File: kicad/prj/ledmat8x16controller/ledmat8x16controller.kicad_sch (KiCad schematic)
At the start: 13 parts, among them J1 Conn_02x08_Odd_Even, J2 Conn_01x02, J3 Conn_01x02_Pin, J4 Conn_01x02_Pin, J6 Conn_01x02_Pin, J8 Conn_01x09_Pin, SW2 SW_Push

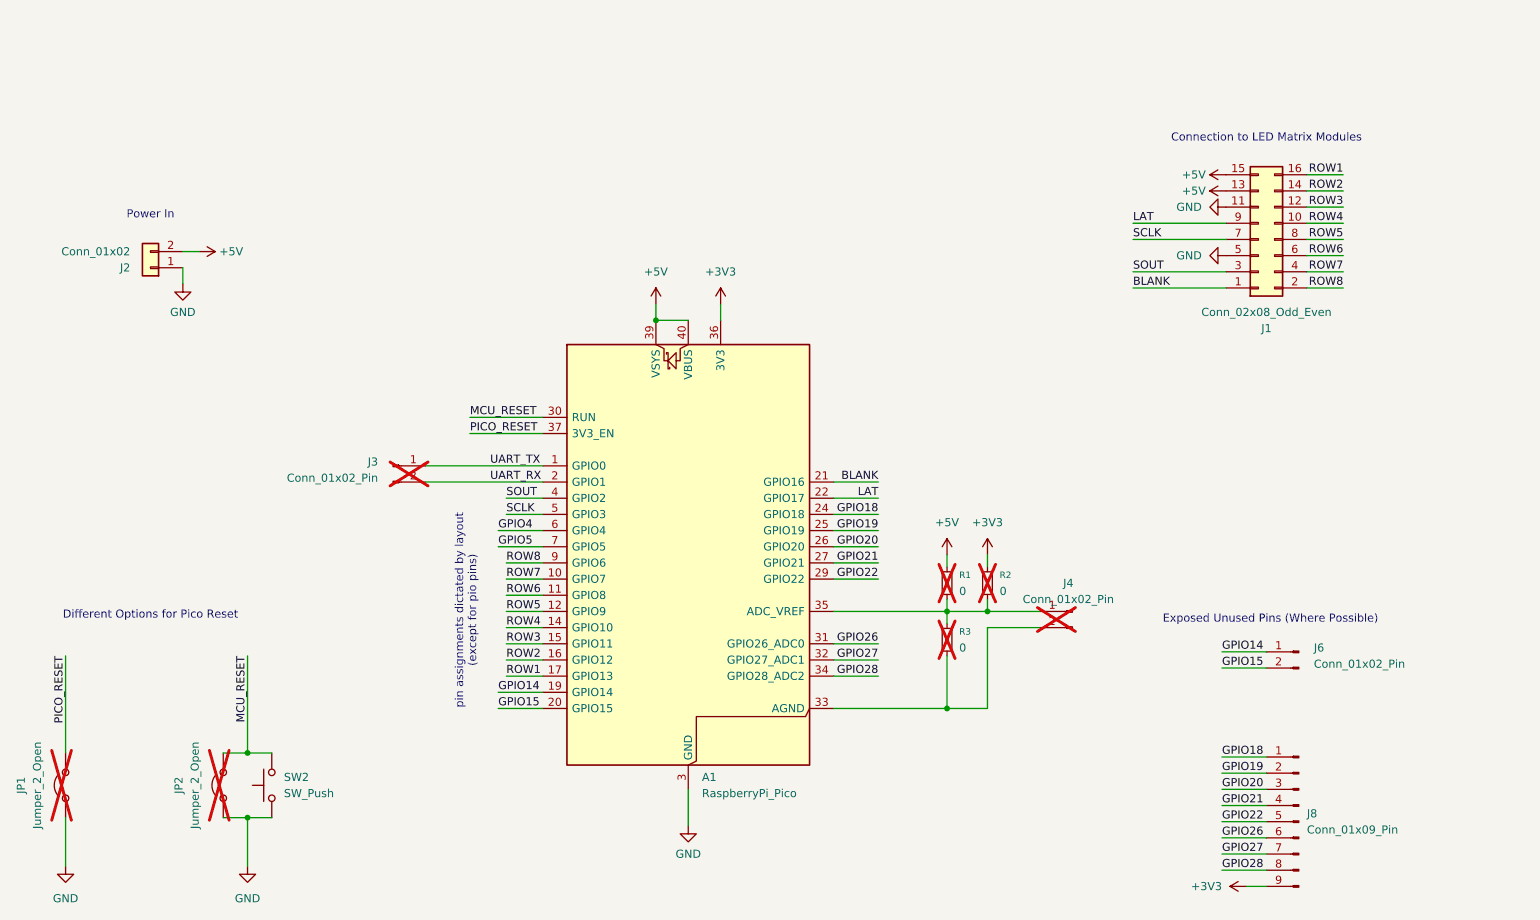
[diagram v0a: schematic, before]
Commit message: Rework the controller (pico carrier) board
Previous version was thrown together in a short time as I was ordering
boards anyways and wanted to test the concept for a pico carrier thing.
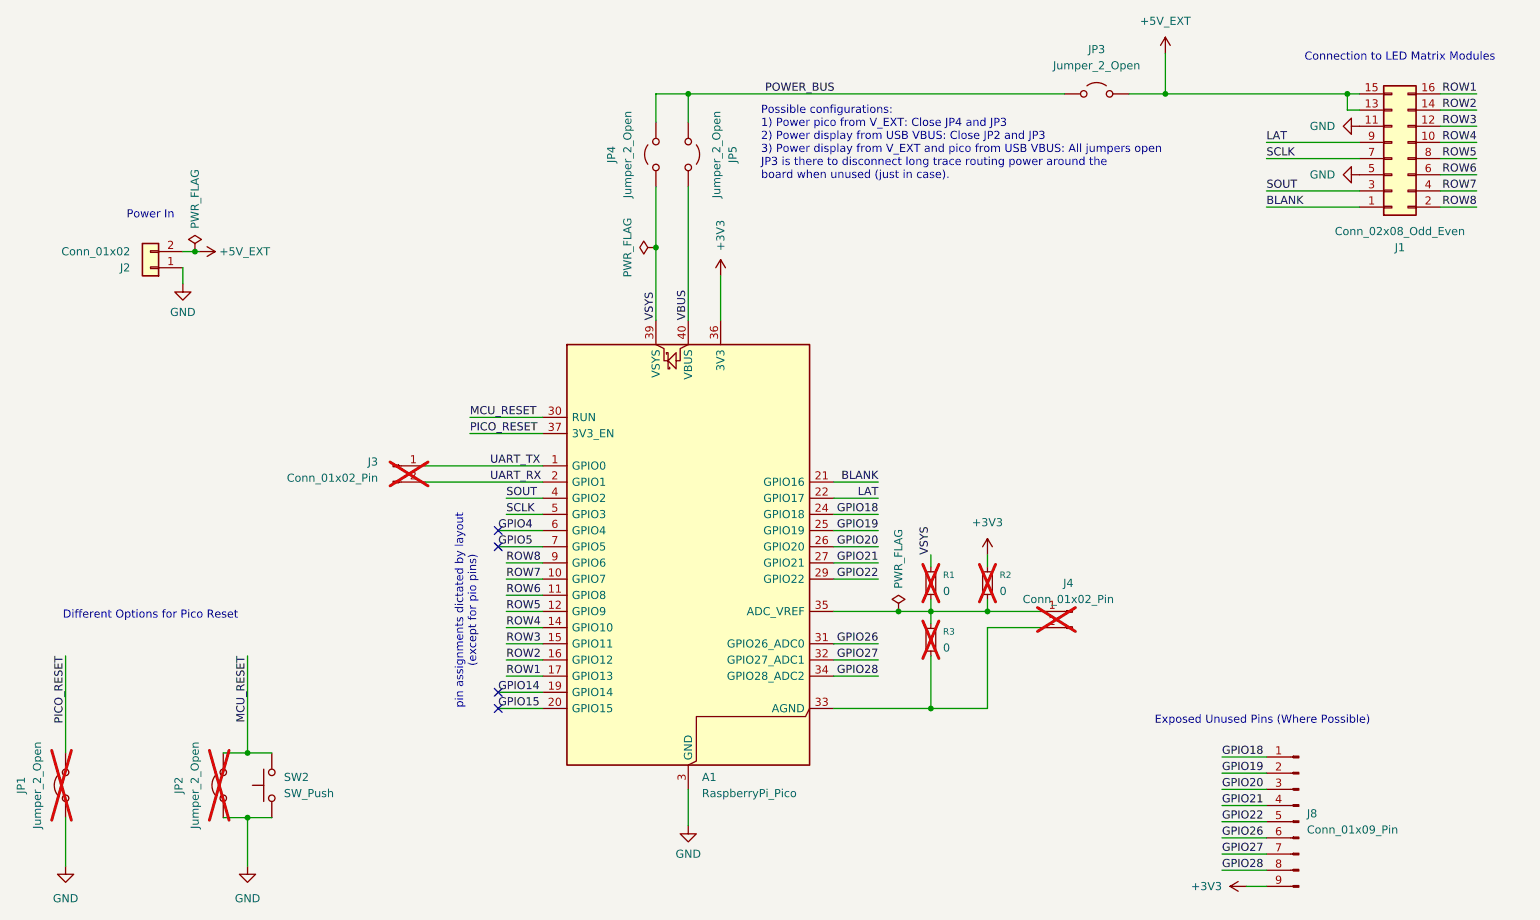
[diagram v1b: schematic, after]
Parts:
- removed J6: Conn_01x02_Pin, Connector_PinHeader_2.54mm:PinHeader_1x02_P2.54mm_Vertical, symbol Connector:Conn_01x02_Pin
- added JP3, JP4, JP5: Jumper_2_Open, Jumper:SolderJumper-2_P1.3mm_Open_RoundedPad1.0x1.5mm, symbol Jumper:Jumper_2_Open
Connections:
- net +5V renamed +5V_EXT
- net +5V_EXT: now also JP3.2 (B); no longer A1.39 (VSYS), A1.40 (VBUS), R1.1
- new net POWER_BUS: JP3.1 (A), JP4.2 (B), JP5.2 (B)
- new net VBUS: A1.40 (VBUS), JP5.1 (A)
- new net VSYS: A1.39 (VSYS), JP4.1 (A), R1.1
- no-connect marks 0 -> 4
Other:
- note added: "Possible configurations: 1) Power pico from V_EXT: Close JP4 and JP3 2) Power display from USB VBUS: Close JP2 and JP3 3) Power display from V_EXT and pico from USB VBUS: All jumpers open JP3 is there to disconnect long trace routing power around the board when unused (just in case)."
- moved on the sheet: J1, R1, R3
